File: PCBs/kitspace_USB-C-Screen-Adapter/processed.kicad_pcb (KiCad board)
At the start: 4 copper layers, 40 x 20.8 mm, 65 parts, among them J1 USB_C_Receptacle, P1 TC2030-CTX-Tag-Connect, Q1 2N7002, Q2 2N7002, SW1 DFU, U1 SY7200AABC, U2 SY7200AABC, U3 STM32F072CBUx, U4 AP2204R-3.3, U5 USBLC6-4, U6 5022505191, U7 STG3684A

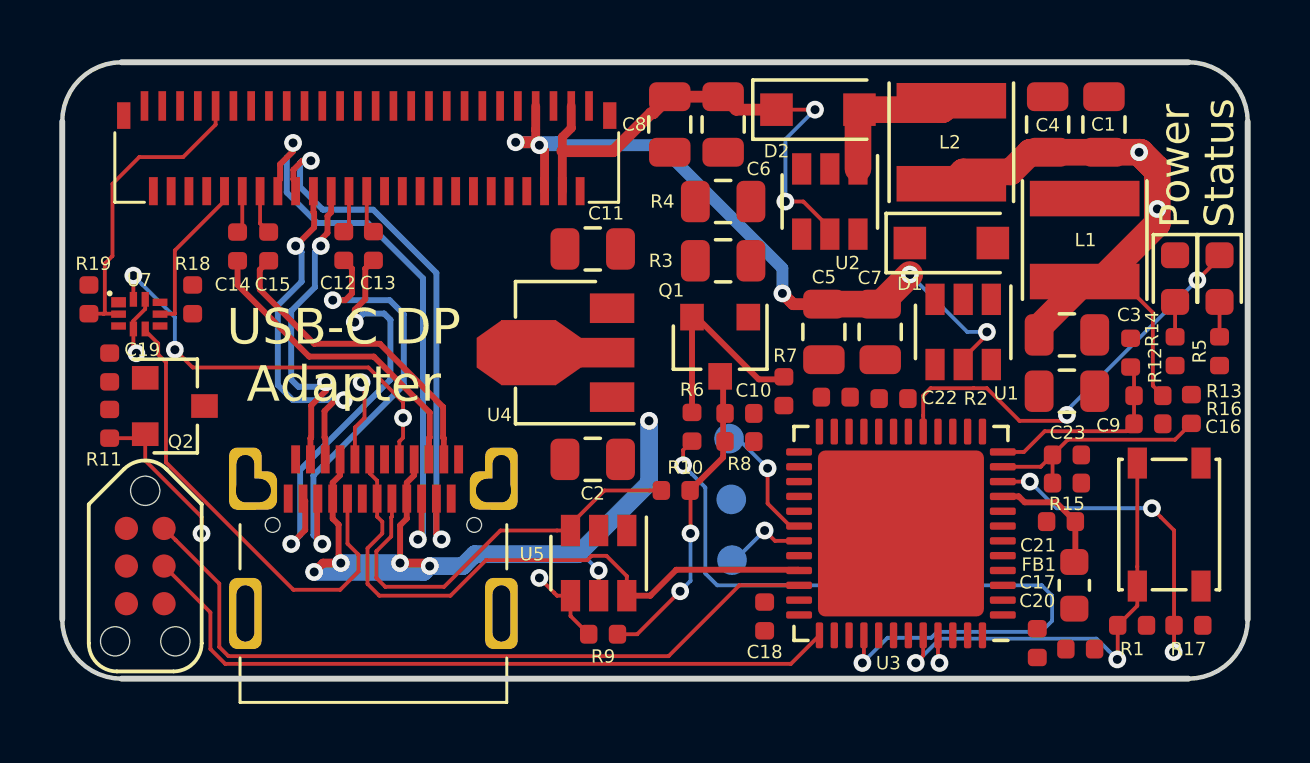
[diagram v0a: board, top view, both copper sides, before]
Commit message: recheck all circuits and clean up fill zone by rerouting the nets using freerouting and manually
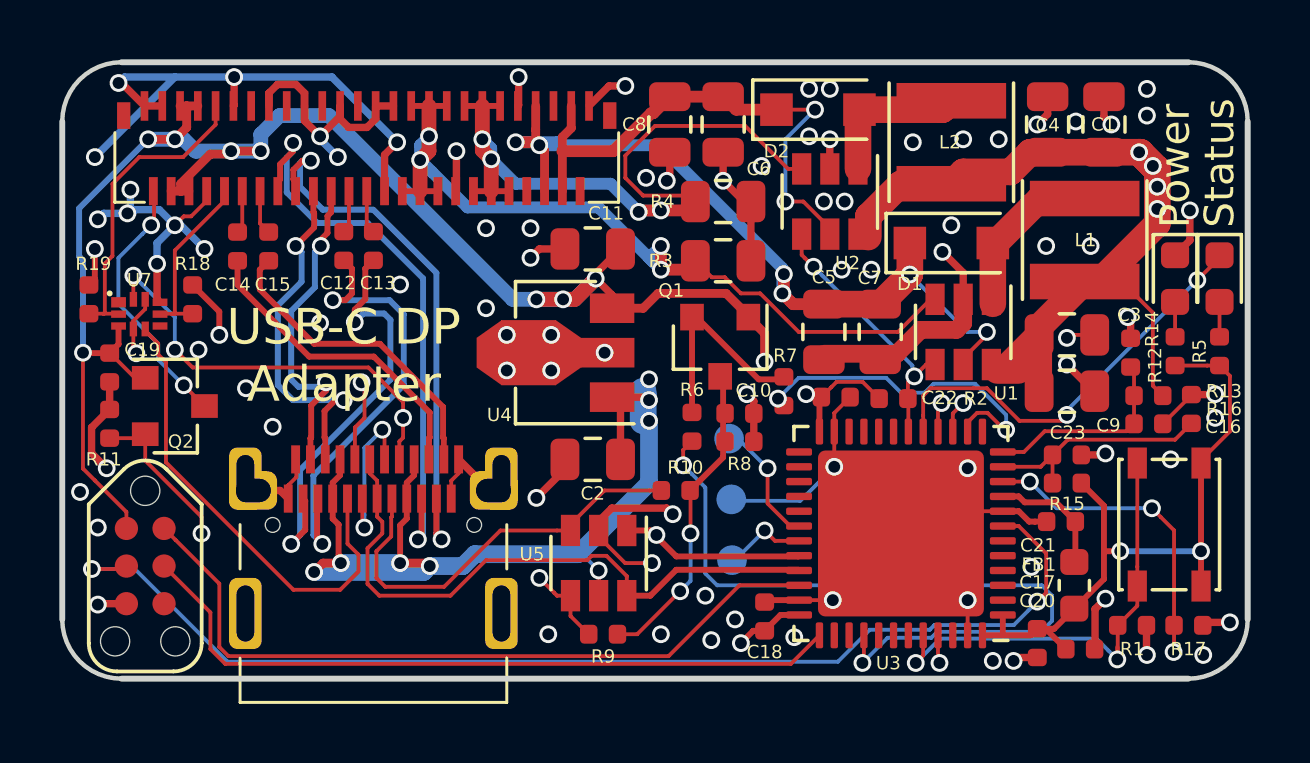
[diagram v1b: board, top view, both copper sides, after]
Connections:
- C1 pad 2: (no net) -> GND
- C10 pad 1: (no net) -> Net-(C10-Pad1)
- C10 pad 2: (no net) -> GND
- C11 pad 1: (no net) -> +3V3
- C11 pad 2: (no net) -> GND
- C16 pad 2: (no net) -> GND
- C17 pad 1: (no net) -> +3V3
- C17 pad 2: (no net) -> GND
- C18 pad 1: (no net) -> +3V3
- C18 pad 2: (no net) -> GND
- C19 pad 1: (no net) -> +3V3
- C19 pad 2: (no net) -> GND
- C2 pad 1: (no net) -> +5V
- C2 pad 2: (no net) -> GND
- C20 pad 1: (no net) -> +3V3
- C20 pad 2: (no net) -> GND
- C21 pad 2: (no net) -> GND
- C22 pad 1: (no net) -> +3V3
- C22 pad 2: (no net) -> GND
- C23 pad 2: (no net) -> GND
- C3 pad 2: (no net) -> GND
- C4 pad 2: (no net) -> GND
- C5 pad 2: (no net) -> GND
- C6 pad 2: (no net) -> GND
- C7 pad 2: (no net) -> GND
- C8 pad 2: (no net) -> GND
- C9 pad 1: (no net) -> +5V
- C9 pad 2: (no net) -> GND
- D1 pad 1: (no net) -> LEDA2
- D1 pad 2: (no net) -> Net-(D1-Pad2)
- D4 pad 1: (no net) -> GND
- FB1 pad 2: (no net) -> +3V3
- J1 pad A1: (no net) -> GND
- J1 pad A12: (no net) -> GND
- J1 pad A7: (no net) -> USB_N
- J1 pad B1: (no net) -> GND
- J1 pad B12: (no net) -> GND
- J1 pad B7: (no net) -> USB_N
- J1 pad S1: (no net) -> GND
- L1 pad 2: (no net) -> Net-(D1-Pad2)
- P1 pad 1: (no net) -> +3V3
- P1 pad 3: (no net) -> NRST
- P1 pad 5: (no net) -> GND
- P1 pad 6: (no net) -> Net-(P1-Pad6)
- Q1 pad 1: (no net) -> +3V3
- Q2 pad 1: (no net) -> +3V3
- Q2 pad 3: (no net) -> HPD
- R1 pad 1: (no net) -> GND
- R11 pad 1: (no net) -> GND
- R12 pad 2: (no net) -> +3V3
- R13 pad 1: (no net) -> VBUS_SENSE
- R14 pad 1: (no net) -> GND
- R15 pad 2: (no net) -> +3V3
- R16 pad 1: (no net) -> GND
- R17 pad 1: (no net) -> GND
- R18 pad 1: (no net) -> AUX_N
- R18 pad 2: (no net) -> _DP_AUX_N
- R19 pad 2: (no net) -> _DP_AUX_P
- R2 pad 1: (no net) -> +3V3
- R2 pad 2: (no net) -> PWM
- R3 pad 1: (no net) -> LEDC2
- R3 pad 2: (no net) -> GND
- R4 pad 1: (no net) -> LEDC1
- R4 pad 2: (no net) -> GND
- R5 pad 2: (no net) -> +3V3
- R7 pad 2: (no net) -> CC_RX
- R8 pad 1: (no net) -> Net-(C10-Pad1)
- R8 pad 2: (no net) -> GND
- SW1 pad 2: (no net) -> +3V3
- TP3 pad 1: (no net) -> GND
- U1 pad 1: (no net) -> Net-(D1-Pad2)
- U1 pad 2: (no net) -> GND
- U1 pad 3: (no net) -> LEDC2
- U1 pad 4: (no net) -> PWM
- U1 pad 6: (no net) -> +5V
- U2 pad 2: (no net) -> GND
- U2 pad 3: (no net) -> LEDC1
- U2 pad 4: (no net) -> PWM
- U2 pad 6: (no net) -> +5V
- U3 pad 1: (no net) -> +3V3
- U3 pad 13: (no net) -> Net-(U3-Pad13)
- U3 pad 14: (no net) -> CC_RX
- U3 pad 15: (no net) -> _DP_AUX_N
- U3 pad 16: (no net) -> _DP_AUX_P
- U3 pad 18: (no net) -> PWM
- U3 pad 19: (no net) -> Net-(U3-Pad19)
- U3 pad 2: (no net) -> Net-(U3-Pad2)
- U3 pad 20: (no net) -> Net-(U3-Pad20)
- U3 pad 21: (no net) -> Net-(U3-Pad21)
- U3 pad 22: (no net) -> Net-(U3-Pad22)
- U3 pad 23: (no net) -> GND
- U3 pad 24: (no net) -> +3V3
- U3 pad 25: (no net) -> Net-(U3-Pad25)
- U3 pad 26: (no net) -> Net-(U3-Pad26)
- U3 pad 27: (no net) -> Net-(U3-Pad27)
- U3 pad 28: (no net) -> Net-(U3-Pad28)
- U3 pad 29: (no net) -> Net-(U3-Pad29)
- U3 pad 3: (no net) -> Net-(U3-Pad3)
- U3 pad 32: (no net) -> USB_N
- U3 pad 35: (no net) -> GND
- U3 pad 36: (no net) -> +3V3
- U3 pad 38: (no net) -> Net-(U3-Pad38)
- U3 pad 39: (no net) -> Net-(U3-Pad39)
- U3 pad 4: (no net) -> Net-(U3-Pad4)
- U3 pad 41: (no net) -> Net-(U3-Pad41)
- U3 pad 42: (no net) -> Net-(U3-Pad42)
- U3 pad 43: (no net) -> Net-(U3-Pad43)
- U3 pad 46: (no net) -> Net-(U3-Pad46)
- U3 pad 47: (no net) -> GND
- U3 pad 48: (no net) -> +3V3
- U3 pad 49: (no net) -> GND
- U3 pad 5: (no net) -> Net-(U3-Pad5)
- U3 pad 6: (no net) -> Net-(U3-Pad6)
- U3 pad 7: (no net) -> NRST
- U3 pad 8: (no net) -> GND
- U4 pad 1: (no net) -> +5V
- U4 pad 2: (no net) -> GND
- U4 pad 3: (no net) -> +3V3
- U5 pad 1: (no net) -> USB_N
- U5 pad 2: (no net) -> GND
- U6 pad 1: (no net) -> GND
- U6 pad 11: (no net) -> GND
- U6 pad 15: (no net) -> GND
- U6 pad 19: (no net) -> GND
- U6 pad 2: (no net) -> HPD
- U6 pad 23: (no net) -> GND
- U6 pad 27: (no net) -> GND
- U6 pad 28: (no net) -> GND
- U6 pad 29: (no net) -> GND
- U6 pad 3: (no net) -> GND
- U6 pad 30: (no net) -> LEDC2
- U6 pad 31: (no net) -> LEDC2
- U6 pad 32: (no net) -> LEDC2
- U6 pad 33: (no net) -> LEDC2
- U6 pad 34: (no net) -> LEDC2
- U6 pad 35: (no net) -> LEDC2
- U6 pad 36: (no net) -> GND
- U6 pad 37: (no net) -> LEDC1
- U6 pad 38: (no net) -> LEDC1
- U6 pad 39: (no net) -> LEDC1
- U6 pad 4: (no net) -> +3V3
- U6 pad 40: (no net) -> LEDC1
- U6 pad 41: (no net) -> LEDC1
- U6 pad 42: (no net) -> LEDC1
- U6 pad 43: (no net) -> GND
- U6 pad 5: (no net) -> +3V3
- U6 pad 51: (no net) -> GND
- U6 pad 6: (no net) -> +3V3
- U6 pad 7: (no net) -> +3V3
- U6 pad 8: (no net) -> GND
- U7 pad 1: (no net) -> Net-(U7-Pad1)
- U7 pad 3: (no net) -> +3V3
- U7 pad 6: (no net) -> Net-(U7-Pad6)
- U7 pad 8: (no net) -> GND
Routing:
- net GND: track 0.00 -> 290.0 mm, vias 0 -> 86
- net +3V3: track 0.00 -> 116.7 mm, vias 0 -> 13
- net NRST: track 0.00 -> 38.8 mm, vias 0 -> 2
- net _DP_AUX_P: track 0.00 -> 36.1 mm, vias 0 -> 2
- net _DP_AUX_N: track 0.00 -> 32.0 mm, vias 0 -> 2
- net LEDC2: track 0.00 -> 28.3 mm, vias 0 -> 4
- net LEDC1: track 0.00 -> 25.1 mm, vias 0 -> 4
- net USB_N: track 0.00 -> 23.5 mm, vias 0 -> 3
- net +5V: track 71.6 -> 86.2 mm, vias 8 -> 12
- net CC_RX: track 0.00 -> 11.2 mm, vias 0 -> 2
- net HPD: track 0.00 -> 9.12 mm, vias 0 -> 2
- net PWM: track 0.00 -> 8.78 mm, vias 0 -> 2
- net Net-(D1-Pad2): track 0.00 -> 5.71 mm
- net LEDA2: track 25.8 -> 27.5 mm, vias 5 -> 6
- net AUX_N: track 5.34 -> 5.94 mm
